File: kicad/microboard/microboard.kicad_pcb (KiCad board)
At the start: 2 copper layers, 14.5 x 9.5 mm, 5 parts, among them J1 Conn_01x04_Socket, U1 TMP235A4DCKR, U2 DRV5011ADDBZR

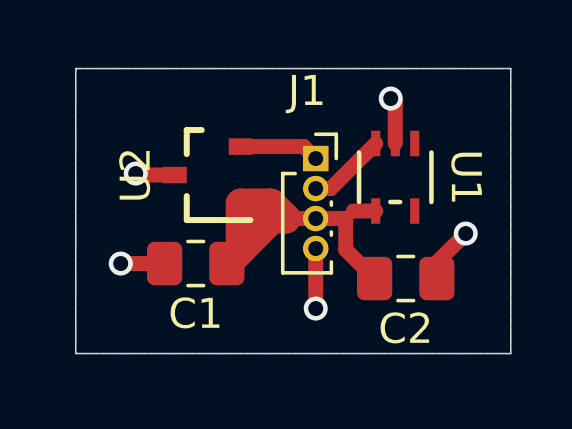
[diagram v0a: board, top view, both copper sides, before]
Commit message: update microboard for current 5-pin connector
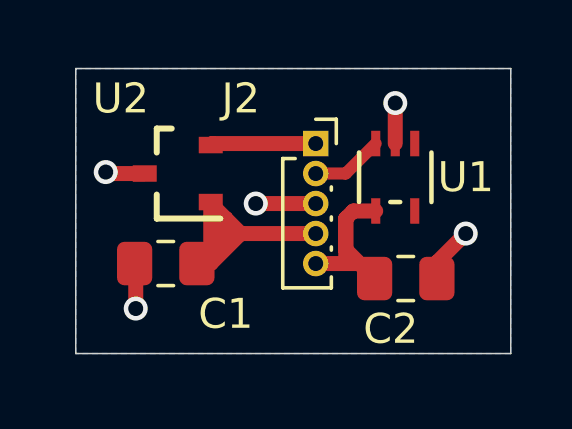
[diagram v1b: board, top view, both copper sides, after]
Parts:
- removed J1: Conn_01x04_Socket, Connector_PinSocket_1.00mm:PinSocket_1x04_P1.00mm_Vertical
- added J2: Conn_01x05_Socket, Connector_PinSocket_1.00mm:PinSocket_1x05_P1.00mm_Vertical, F.Cu at (154.5, 87.5)
- moved U2 1.00 mm to (149.9, 88.5)
- moved C1 1.00 mm to (149.5, 91.5)
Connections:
- C1 pad 1: /+5VA -> /+3.3V
- U2 pad 1: /+5VA -> /+3.3V
- U2 pad 2: /HallAnalog -> /Hall
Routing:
- net /+3.3V: track 0.00 -> 9.98 mm
- net /+5VA: track 12.0 -> 7.17 mm
- net /Hall: track 0.00 -> 3.52 mm
- net /HallAnalog: track 2.67 -> 0.00 mm

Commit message: beefier capacitors on the microboard
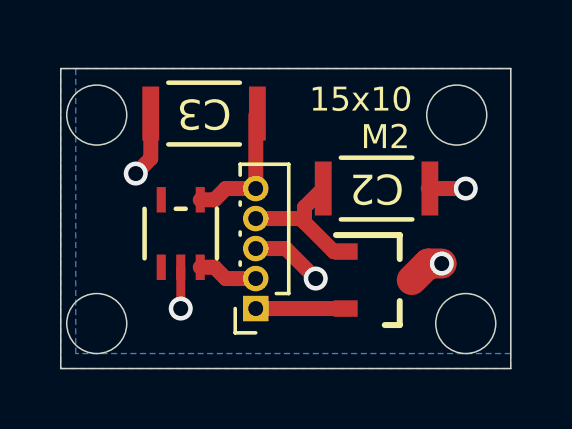
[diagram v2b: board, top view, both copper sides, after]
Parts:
- removed C1: .01u, Capacitor_SMD:C_0805_2012Metric_Pad1.18x1.45mm_HandSolder
- added C3: .1u, dank:CAP_3216_TDK, F.Cu at (150.8, 86.5)
- C2: value .1u -> .01u; footprint Capacitor_SMD:C_0805_2012Metric_Pad1.18x1.45mm_HandSolder -> dank:CAP_3216_TDK
- moved U2 7.58 mm to (156.6, 92.1), turned to 0 degrees
- moved U1 7.39 mm to (150.0, 90.5), turned to 90 degrees
- moved J2 5.85 mm to (152.5, 93.0), turned to 180 degrees
- moved C2 3.15 mm to (156.5, 89.0)
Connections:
- C2 pad 2: /+5VA -> /+3.3V
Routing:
- net /+3.3V: track 9.98 -> 4.84 mm
- net /+5VA: track 7.17 -> 4.44 mm
- net /Hall: track 3.52 -> 3.00 mm
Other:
- board size 14.5 x 9.5 mm -> 15 x 10 mm
- board text added: "15x10"
- board text added: "M2"
